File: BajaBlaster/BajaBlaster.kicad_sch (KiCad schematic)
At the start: 0 parts

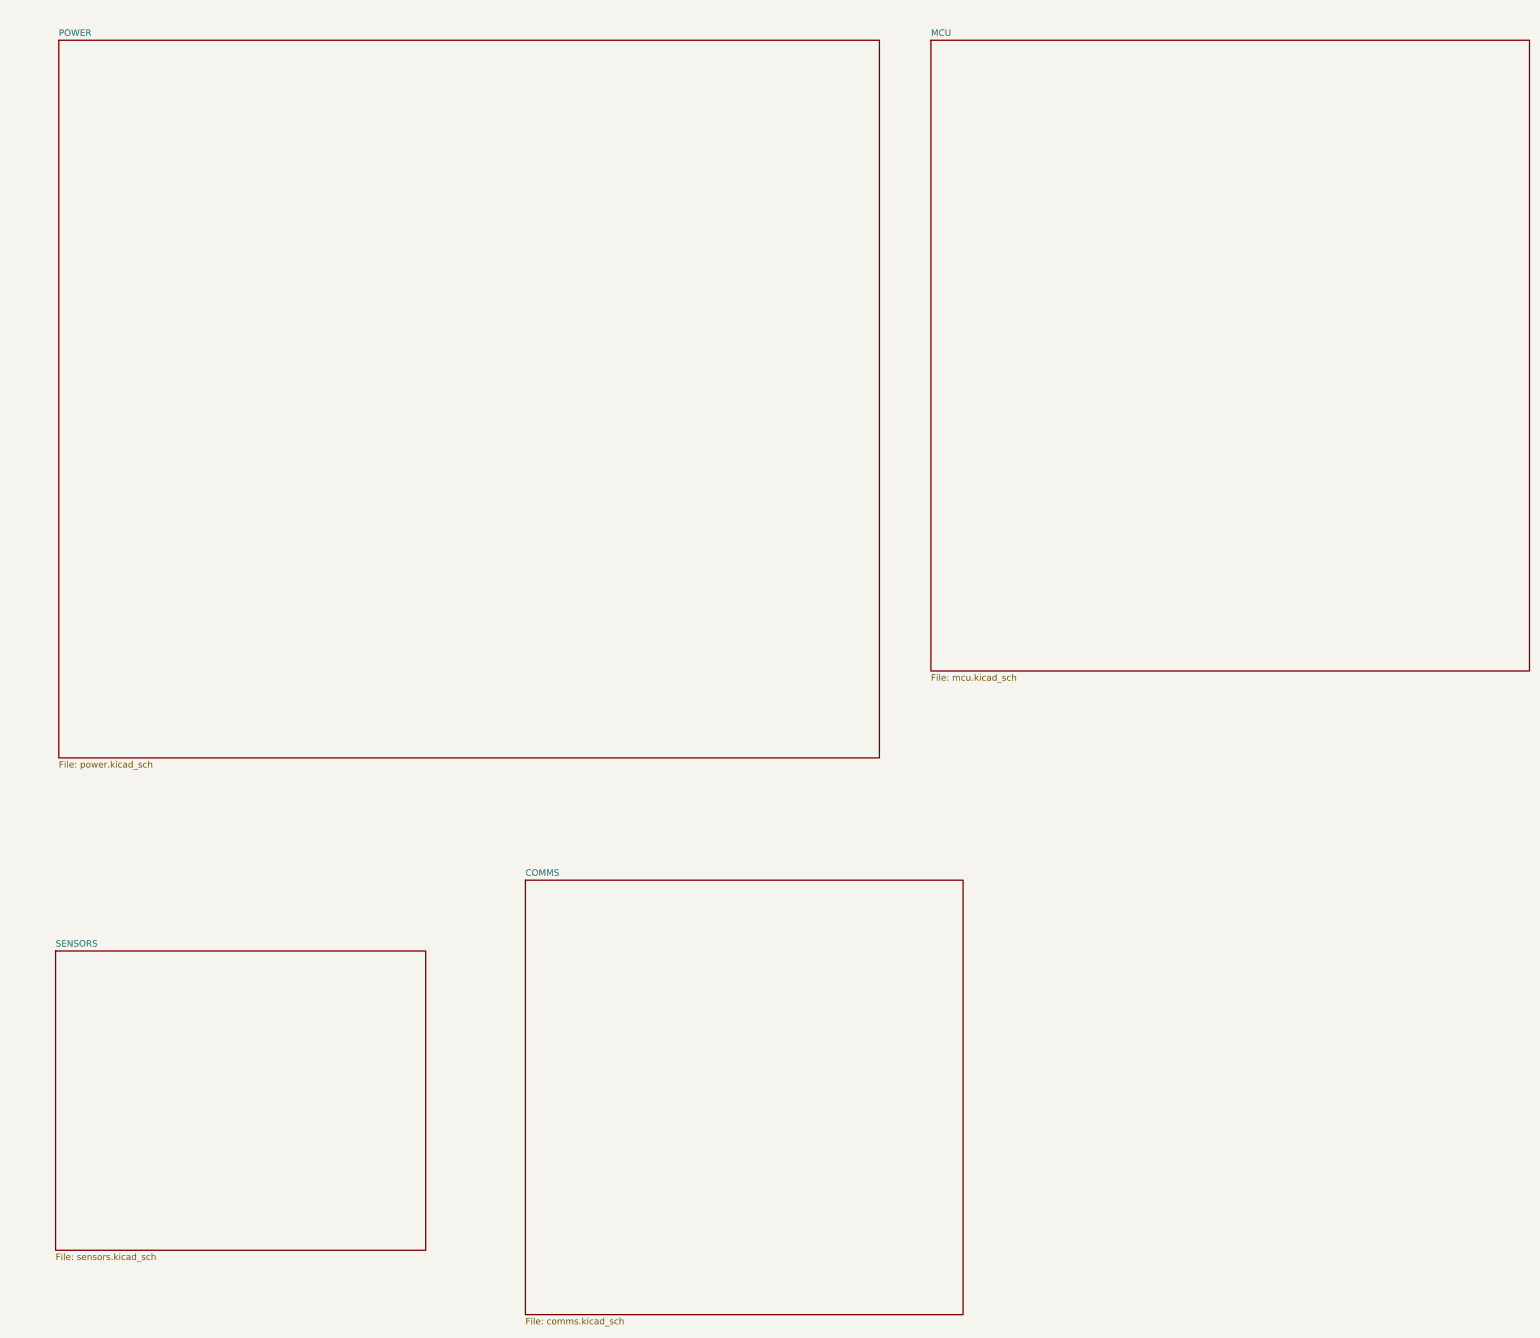
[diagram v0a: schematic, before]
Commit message: got the heirarchical labels all connected and removed the sensor subsheet because its gonna be merged with the mcu subsheet
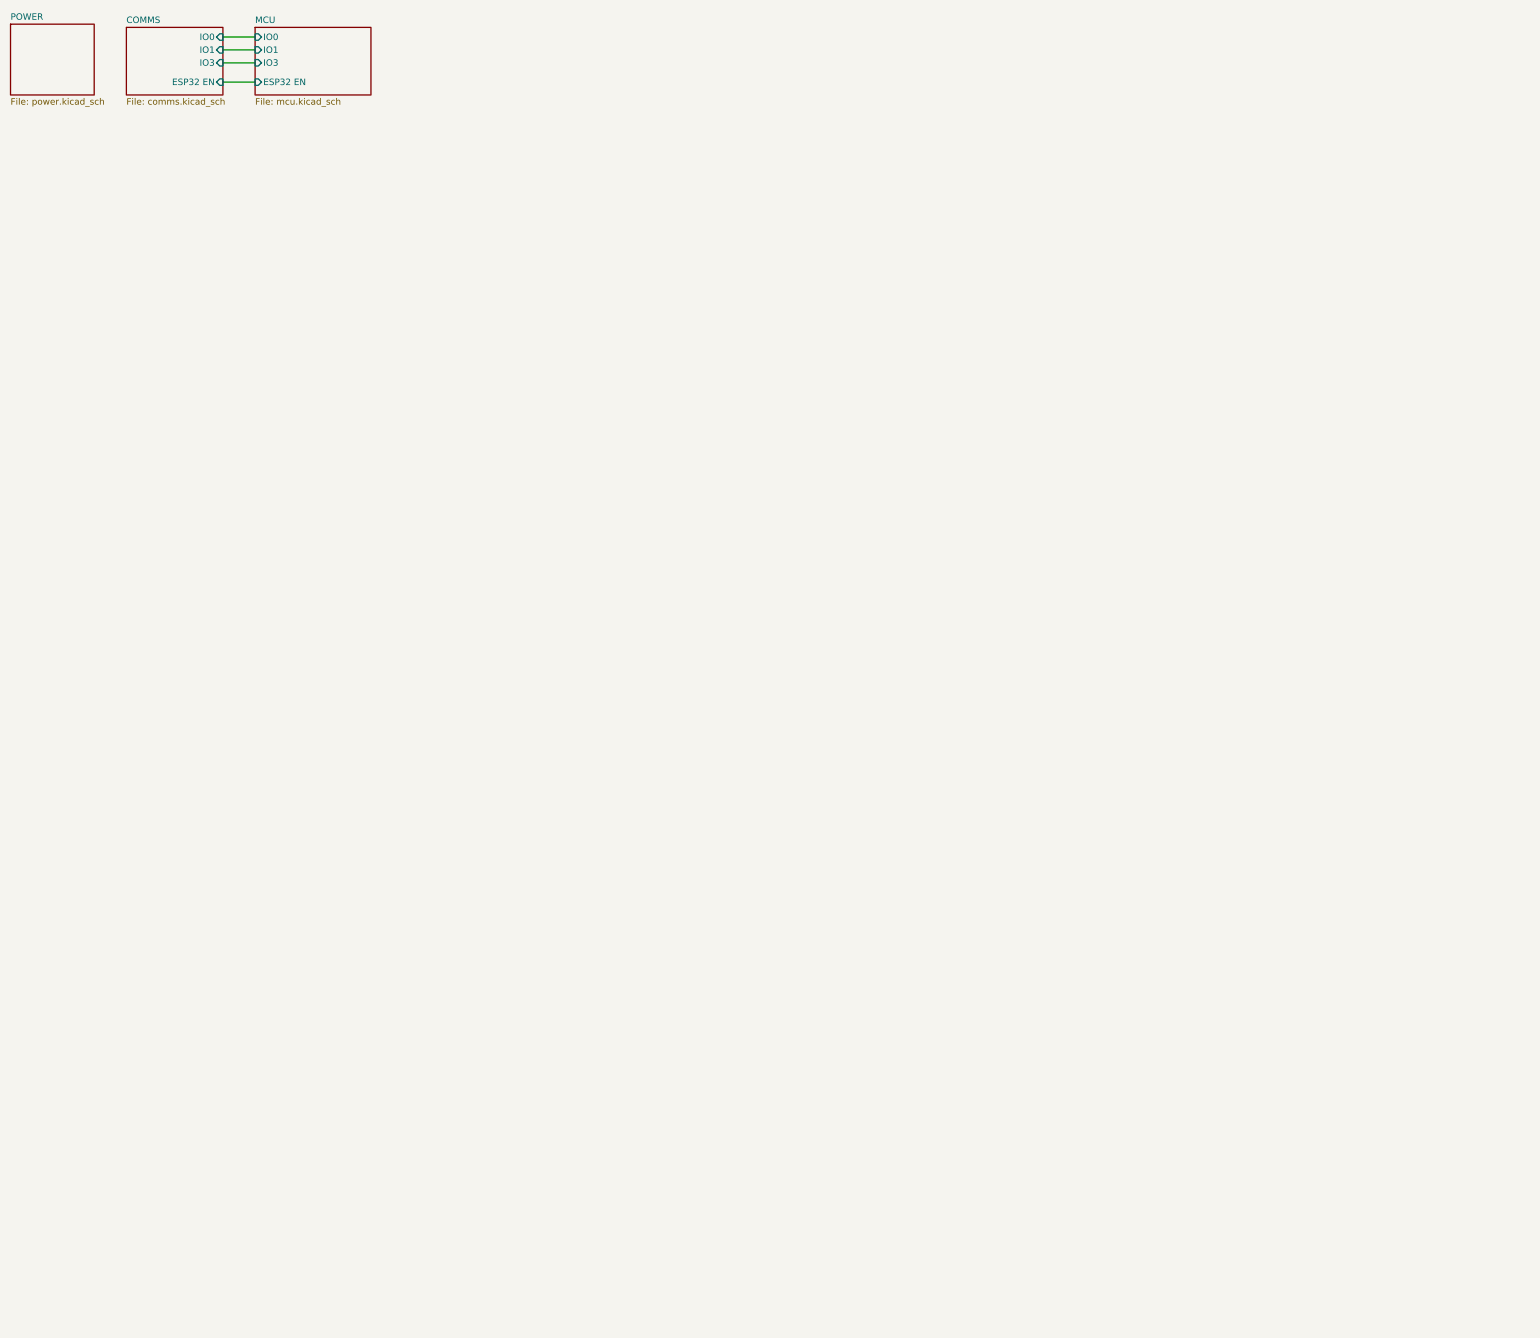
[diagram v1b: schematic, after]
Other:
- removed sheet SENSORS
- sheet COMMS ports: added ESP32 EN, IO0, IO1, IO3; removed none
- sheet MCU ports: added ESP32 EN, IO0, IO1, IO3; removed none
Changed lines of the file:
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@@
 	(generator "eeschema")
 	(generator_version "10.0")
-	(paper "A3")
+	(paper "A5")
+	(wire
+		(pts
+			(xy 58.42 25.4) (xy 64.77 25.4)
+		)
+		(stroke
+			(width 0)
+			(type default)
+		)
+	)
+	(wire
+		(pts
+			(xy 58.42 29.21) (xy 64.77 29.21)
+		)
+		(stroke
+			(width 0)
+			(type default)
+		)
+	)
+	(wire
+		(pts
+			(xy 58.42 20.32) (xy 64.77 20.32)
+		)
+		(stroke
+			(width 0)
+			(type default)
+		)
+	)
+	(wire
+		(pts
+			(xy 58.42 22.86) (xy 64.77 22.86)
+		)
+		(stroke
+			(width 0)
+			(type default)
+		)
+	)
 	(sheet
-		(at 25.4 200.66)
-		(size 73.025 59.055)
+		(at 39.37 18.415)
+		(size 19.05 13.335)
 		(exclude_from_sim no)
 		(in_bom yes)
@@
 			(color 0 0 0 0)
 		)
-		(property "Sheetname" "SENSORS"
-			(at 25.4 199.9484 0)
+		(property "Sheetname" "COMMS"
+			(at 39.37 17.7034 0)
 			(show_name no)
 			(do_not_autoplace no)
@@
 			)
 		)
-		(property "Sheetfile" "sensors.kicad_sch"
-			(at 25.4 260.2996 0)
+		(property "Sheetfile" "comms.kicad_sch"
+			(at 39.37 32.3346 0)
 			(show_name no)
 			(do_not_autoplace no)
@@
 				)
 				(justify left top)
+			)
+		)
+		(pin "IO1" input
+			(at 58.42 22.86 0)
+			(effects
+				(font
+					(size 1.27 1.27)
+				)
+				(justify right)
+			)
+		)
+		(pin "IO3" input
+			(at 58.42 25.4 0)
+			(effects
+				(font
+					(size 1.27 1.27)
+				)
+				(justify right)
+			)
+		)
+		(pin "ESP32 EN" input
+			(at 58.42 29.21 0)
+			(effects
+				(font
+					(size 1.27 1.27)
+				)
+				(justify right)
+			)
+		)
+		(pin "IO0" input
+			(at 58.42 20.32 0)
+			(effects
+				(font
+					(size 1.27 1.27)
+				)
+				(justify right)
 			)
 		)
@@
 			(project "BajaBlaster"
 				(path "/08a0edf5-ad57-4ef4-97bf-c48cb466bb64"
-					(page "4")
+					(page "5")
 				)
 			)
@@
 	)
 	(sheet
-		(at 118.11 186.69)
-		(size 86.36 85.725)
+		(at 16.51 17.78)
+		(size 16.51 13.97)
 		(exclude_from_sim no)
 		(in_bom yes)
@@
 			(color 0 0 0 0)
 		)
-		(property "Sheetname" "COMMS"
-			(at 118.11 185.9784 0)
+		(property "Sheetname" "POWER"
+			(at 16.51 17.0684 0)
 			(show_name no)
 			(do_not_autoplace no)
@@
 			)
 		)
-		(property "Sheetfile" "comms.kicad_sch"
-			(at 118.11 272.9996 0)
+		(property "Sheetfile" "power.kicad_sch"
+			(at 16.51 32.3346 0)
 			(show_name no)
 			(do_not_autoplace no)
@@
 			(project "BajaBlaster"
 				(path "/08a0edf5-ad57-4ef4-97bf-c48cb466bb64"
-					(page "5")
+					(page "2")
 				)
 			)
@@
 	)
 	(sheet
-		(at 26.035 20.955)
-		(size 161.925 141.605)
+		(at 64.77 18.415)
+		(size 22.86 13.335)
 		(exclude_from_sim no)
 		(in_bom yes)
@@
 			(color 0 0 0 0)
 		)
-		(property "Sheetname" "POWER"
-			(at 26.035 20.2434 0)
+		(property "Sheetname" "MCU"
+			(at 64.77 17.7034 0)
 			(show_name no)
 			(do_not_autoplace no)
@@
 			)
 		)
-		(property "Sheetfile" "power.kicad_sch"
-			(at 26.035 163.1446 0)
+		(property "Sheetfile" "mcu.kicad_sch"
+			(at 64.77 32.3346 0)
 			(show_name no)
 			(do_not_autoplace no)
@@
 			)
 		)
-		(instances
-			(project "BajaBlaster"
-				(path "/08a0edf5-ad57-4ef4-97bf-c48cb466bb64"
-					(page "2")
-				)
-			)
-		)
-	)
-	(sheet
-		(at 198.12 20.955)
-		(size 118.11 124.46)
-		(exclude_from_sim no)
-		(in_bom yes)
-		(on_board yes)
-		(dnp no)
-		(fields_autoplaced yes)
-		(stroke
-			(width 0.1524)
-			(type solid)
-		)
-		(fill
-			(color 0 0 0 0)
-		)
-		(property "Sheetname" "MCU"
-			(at 198.12 20.2434 0)
-			(show_name no)
-			(do_not_autoplace no)
-			(effects
-				(font
-					(size 1.27 1.27)
-				)
-				(justify left bottom)
-			)
-		)
-		(property "Sheetfile" "mcu.kicad_sch"
-			(at 198.12 145.9996 0)
-			(show_name no)
-			(do_not_autoplace no)
-			(effects
-				(font
-					(size 1.27 1.27)
-				)
-				(justify left top)
-			)
-		)
+		(pin "IO1" input
+			(at 64.77 22.86 180)
+			(effects
+				(font
+					(size 1.27 1.27)
+				)
+				(justify left)
+			)
+		)
+		(pin "IO3" input
+			(at 64.77 25.4 180)
+			(effects
+				(font
+					(size 1.27 1.27)
+				)
+				(justify left)
+			)
+		)
+		(pin "IO0" input
+			(at 64.77 20.32 180)
+			(effects
+				(font
+					(size 1.27 1.27)
+				)
+				(justify left)
+			)
+		)
+		(pin "ESP32 EN" input
+			(at 64.77 29.21 180)
+			(effects
+				(font
+					(size 1.27 1.27)
+				)
+				(justify left)
+			)
+		)

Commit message: added new h tags
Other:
- sheet COMMS ports: added CAN_RX, CAN_TX; removed none
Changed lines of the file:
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@@
 	(sheet
 		(at 39.37 18.415)
-		(size 19.05 13.335)
+		(size 19.05 26.67)
 		(exclude_from_sim no)
 		(in_bom yes)
@@
 		)
 		(property "Sheetfile" "comms.kicad_sch"
-			(at 39.37 32.3346 0)
+			(at 39.37 45.6696 0)
 			(show_name no)
 			(do_not_autoplace no)
@@
 		(pin "IO0" input
 			(at 58.42 20.32 0)
+			(effects
+				(font
+					(size 1.27 1.27)
+				)
+				(justify right)
+			)
+		)
+		(pin "CAN_TX" input
+			(at 58.42 38.1 0)
+			(effects
+				(font
+					(size 1.27 1.27)
+				)
+				(justify right)
+			)
+		)
+		(pin "CAN_RX" input
+			(at 58.42 35.56 0)
 			(effects
 				(font
@@
 	(sheet
 		(at 64.77 18.415)
-		(size 22.86 13.335)
+		(size 19.685 26.67)
 		(exclude_from_sim no)
 		(in_bom yes)
@@
 		)
 		(property "Sheetfile" "mcu.kicad_sch"
-			(at 64.77 32.3346 0)
+			(at 64.77 45.6696 0)
 			(show_name no)
 			(do_not_autoplace no)

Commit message: doing lots of small tweaks and fixups
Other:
- sheet COMMS ports: added ESP32_EN, INTERBOARD_RX, INTERBOARD_TX, SYNC, U0RXD, U0TXD; removed ESP32 EN, IO0, IO1, IO3
- sheet MCU ports: added CAN_RX, CAN_TX, ESP32_EN, INTERBOARD_RX, INTERBOARD_TX, SYNC, U0RXD, U0TXD; removed ESP32 EN, IO0, IO1, IO3
- title: (none) -> BAJA_BLASTER_REV_A
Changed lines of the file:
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@@
 	(generator_version "10.0")
 	(paper "A5")
-	(wire
-		(pts
-			(xy 58.42 25.4) (xy 64.77 25.4)
-		)
-		(stroke
-			(width 0)
-			(type default)
-		)
-	)
-	(wire
-		(pts
-			(xy 58.42 29.21) (xy 64.77 29.21)
-		)
-		(stroke
-			(width 0)
-			(type default)
-		)
-	)
-	(wire
-		(pts
-			(xy 58.42 20.32) (xy 64.77 20.32)
-		)
-		(stroke
-			(width 0)
-			(type default)
-		)
-	)
-	(wire
-		(pts
-			(xy 58.42 22.86) (xy 64.77 22.86)
+	(title_block
+		(title "BAJA_BLASTER_REV_A")
+	)
+	(wire
+		(pts
+			(xy 99.06 60.96) (xy 105.41 60.96)
+		)
+		(stroke
+			(width 0)
+			(type default)
+		)
+	)
+	(wire
+		(pts
+			(xy 99.06 71.755) (xy 105.41 71.755)
+		)
+		(stroke
+			(width 0)
+			(type default)
+		)
+	)
+	(wire
+		(pts
+			(xy 99.06 48.26) (xy 105.41 48.26)
+		)
+		(stroke
+			(width 0)
+			(type default)
+		)
+	)
+	(wire
+		(pts
+			(xy 99.06 64.135) (xy 105.41 64.135)
+		)
+		(stroke
+			(width 0)
+			(type default)
+		)
+	)
+	(wire
+		(pts
+			(xy 99.06 74.295) (xy 105.41 74.295)
+		)
+		(stroke
+			(width 0)
+			(type default)
+		)
+	)
+	(wire
+		(pts
+			(xy 99.06 52.07) (xy 105.41 52.07)
+		)
+		(stroke
+			(width 0)
+			(type default)
+		)
+	)
+	(wire
+		(pts
+			(xy 99.06 43.18) (xy 105.41 43.18)
+		)
+		(stroke
+			(width 0)
+			(type default)
+		)
+	)
+	(wire
+		(pts
+			(xy 99.06 45.72) (xy 105.41 45.72)
 		)
 		(stroke
@@
 	)
 	(sheet
-		(at 39.37 18.415)
-		(size 19.05 26.67)
+		(at 80.01 41.275)
+		(size 19.05 34.925)
 		(exclude_from_sim no)
 		(in_bom yes)
@@
 		)
 		(property "Sheetname" "COMMS"
-			(at 39.37 17.7034 0)
+			(at 80.01 40.5634 0)
 			(show_name no)
 			(do_not_autoplace no)
@@
 		)
 		(property "Sheetfile" "comms.kicad_sch"
-			(at 39.37 45.6696 0)
+			(at 80.01 76.7846 0)
 			(show_name no)
 			(do_not_autoplace no)
@@
 			)
 		)
-		(pin "IO1" input
-			(at 58.42 22.86 0)
-			(effects
-				(font
-					(size 1.27 1.27)
-				)
-				(justify right)
-			)
-		)
-		(pin "IO3" input
-			(at 58.42 25.4 0)
-			(effects
-				(font
-					(size 1.27 1.27)
-				)
-				(justify right)
-			)
-		)
-		(pin "ESP32 EN" input
-			(at 58.42 29.21 0)
-			(effects
-				(font
-					(size 1.27 1.27)
-				)
-				(justify right)
-			)
-		)
-		(pin "IO0" input
-			(at 58.42 20.32 0)
-			(effects
-				(font
-					(size 1.27 1.27)
-				)
-				(justify right)
-			)
-		)
-		(pin "CAN_TX" input
-			(at 58.42 38.1 0)
-			(effects
-				(font
-					(size 1.27 1.27)
-				)
-				(justify right)
-			)
-		)
-		(pin "CAN_RX" input
-			(at 58.42 35.56 0)
+		(pin "ESP32_EN" bidirectional
+			(at 99.06 52.07 0)
+			(effects
+				(font
+					(size 1.27 1.27)
+				)
+				(justify right)
+			)
+		)
+		(pin "CAN_TX" bidirectional
+			(at 99.06 74.295 0)
+			(effects
+				(font
+					(size 1.27 1.27)
+				)
+				(justify right)
+			)
+		)
+		(pin "CAN_RX" bidirectional
+			(at 99.06 71.755 0)
+			(effects
+				(font
+					(size 1.27 1.27)
+				)
+				(justify right)
+			)
+		)
+		(pin "U0RXD" bidirectional
+			(at 99.06 43.18 0)
+			(effects
+				(font
+					(size 1.27 1.27)
+				)
+				(justify right)
+			)
+		)
+		(pin "INTERBOARD_RX" bidirectional
+			(at 99.06 60.96 0)
+			(effects
+				(font
+					(size 1.27 1.27)
+				)
+				(justify right)
+			)
+		)
+		(pin "INTERBOARD_TX" bidirectional
+			(at 99.06 64.135 0)
+			(effects
+				(font
+					(size 1.27 1.27)
+				)
+				(justify right)
+			)
+		)
+		(pin "U0TXD" bidirectional
+			(at 99.06 45.72 0)
+			(effects
+				(font
+					(size 1.27 1.27)
+				)
+				(justify right)
+			)
+		)
+		(pin "SYNC" bidirectional
+			(at 99.06 48.26 0)
 			(effects
 				(font
@@
 	)
 	(sheet
-		(at 16.51 17.78)
+		(at 57.15 40.64)
 		(size 16.51 13.97)
 		(exclude_from_sim no)
@@
 		)
 		(property "Sheetname" "POWER"
-			(at 16.51 17.0684 0)
+			(at 57.15 39.9284 0)
 			(show_name no)
 			(do_not_autoplace no)
@@
 		)
 		(property "Sheetfile" "power.kicad_sch"
-			(at 16.51 32.3346 0)
+			(at 57.15 55.1946 0)
 			(show_name no)
 			(do_not_autoplace no)
@@
 	)
 	(sheet
-		(at 64.77 18.415)
-		(size 19.685 26.67)
+		(at 105.41 41.275)
+		(size 19.685 34.925)
 		(exclude_from_sim no)
 		(in_bom yes)
@@
 		)
 		(property "Sheetname" "MCU"
-			(at 64.77 17.7034 0)
+			(at 105.41 40.5634 0)
 			(show_name no)
 			(do_not_autoplace no)
@@
 		)
 		(property "Sheetfile" "mcu.kicad_sch"
-			(at 64.77 45.6696 0)
+			(at 105.41 76.7846 0)
 			(show_name no)
 			(do_not_autoplace no)
@@
 			)
 		)
-		(pin "IO1" input
-			(at 64.77 22.86 180)
-			(effects
-				(font
-					(size 1.27 1.27)
-				)
-				(justify left)
-			)
-		)
-		(pin "IO3" input
-			(at 64.77 25.4 180)
-			(effects
-				(font
-					(size 1.27 1.27)
-				)
-				(justify left)
-			)
-		)
-		(pin "IO0" input
-			(at 64.77 20.32 180)
-			(effects
-				(font
-					(size 1.27 1.27)
-				)
-				(justify left)
-			)
-		)
-		(pin "ESP32 EN" input
-			(at 64.77 29.21 180)
-			(effects
-				(font
+		(pin "ESP32_EN" bidirectional
+			(at 105.41 52.07 180)
+			(effects
+				(font
+					(size 1.27 1.27)
+				)
+				(justify left)
+			)
+		)
+		(pin "U0TXD" bidirectional
+			(at 105.41 45.72 180)
+			(effects
+				(font
+					(size 1.27 1.27)
+				)
+				(justify left)
+			)
+		)
+		(pin "U0RXD" bidirectional
+			(at 105.41 43.18 180)
+			(effects
+				(font
+					(size 1.27 1.27)
+				)
+				(justify left)
+			)
+		)
+		(pin "INTERBOARD_RX" bidirectional
+			(at 105.41 60.96 180)
+			(effects
+				(font
+					(size 1.27 1.27)
+				)
+				(justify left)
+			)
+		)
+		(pin "INTERBOARD_TX" bidirectional
+			(at 105.41 64.135 180)
+			(effects
+				(font
+					(size 1.27 1.27)
+				)
+				(justify left)
+			)
+		)
+		(pin "CAN_RX" bidirectional
+			(at 105.41 71.755 180)
+			(effects
+				(font
+					(size 1.27 1.27)
+				)
+				(justify left)
+			)
+		)
+		(pin "CAN_TX" bidirectional
+			(at 105.41 74.295 180)
+			(effects
+				(font
+					(size 1.27 1.27)
+				)
+				(justify left)
+			)
+		)
+		(pin "SYNC" bidirectional
+			(at 105.41 48.26 180)
+			(effects
+				(font
